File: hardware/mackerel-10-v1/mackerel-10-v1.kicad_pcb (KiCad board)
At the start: 4 copper layers, 150 x 114 mm, 59 parts, among them J1 Conn_02x05_Odd_Even, J10 Conn_01x06, J2 Conn_02x20_Odd_Even, J3 Conn_02x20_Odd_Even, J6 Barrel_Jack_MountingPin, J9 Conn_01x06, SW1 SW_Push, U1 68010D, U3 SST39SF040, U4 AS6C4008-55PCN, U5 SST39SF040, U6 AS6C4008-55PCN, U7 XR68C681, U9 NE555P, X1 50 MHz, X2 3.6864MHz

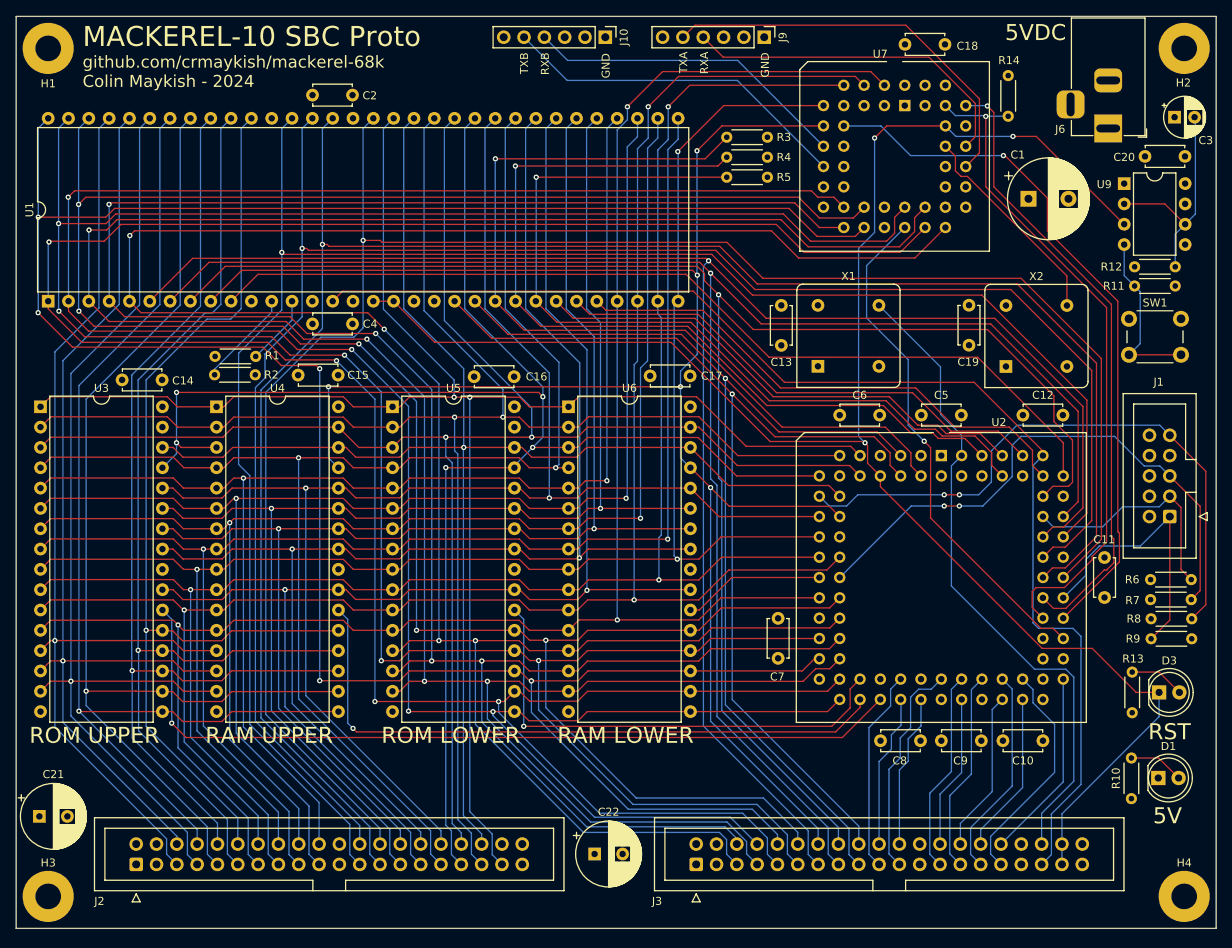
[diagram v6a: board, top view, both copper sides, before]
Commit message: Mack-10 proto routed and passing DRC
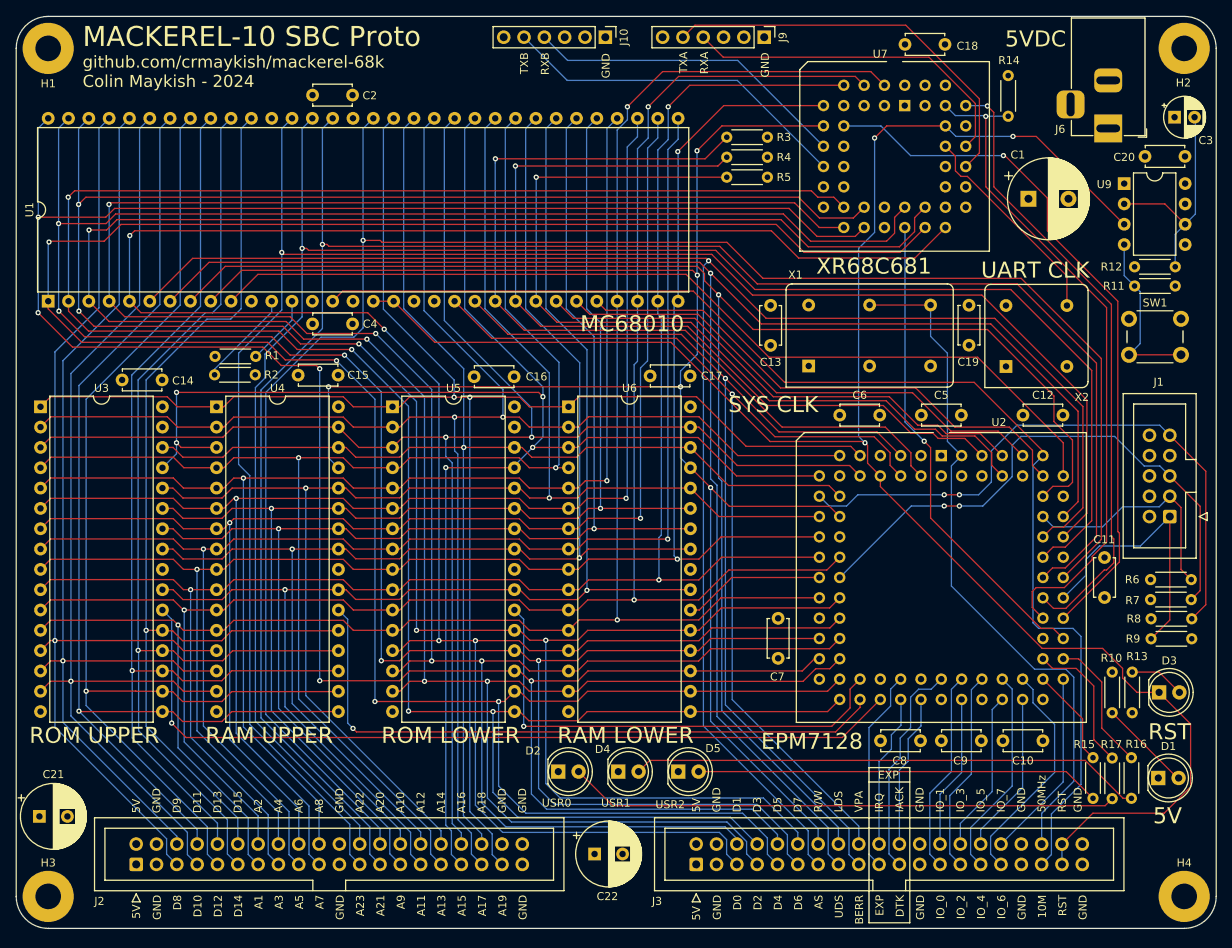
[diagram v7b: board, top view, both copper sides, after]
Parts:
- added D2: LED, LED_THT:LED_D5.0mm, F.Cu at (87.8, 114.4)
- added D4: LED, LED_THT:LED_D5.0mm, F.Cu at (95.3, 114.4)
- added D5: LED, LED_THT:LED_D5.0mm, F.Cu at (102.8, 114.4)
- added R15: R, Resistor_THT:R_Axial_DIN0204_L3.6mm_D1.6mm_P5.08mm_Horizontal, F.Cu at (154.6, 112.7)
- added R16: R, Resistor_THT:R_Axial_DIN0204_L3.6mm_D1.6mm_P5.08mm_Horizontal, F.Cu at (159.4, 112.7)
- added R17: R, Resistor_THT:R_Axial_DIN0204_L3.6mm_D1.6mm_P5.08mm_Horizontal, F.Cu at (157.0, 112.7)
- X1: value 50 MHz -> 50MHz; footprint Oscillator:Oscillator_DIP-8 -> Oscillator:Oscillator_DIP-14
- moved R10 16.0 mm to (157.0, 102.0), turned to -90 degrees
- moved C13 1.34 mm to (114.3, 56.1)
- moved X1 1.16 mm to (119.1, 63.7)
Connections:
- J2 pad 38: unconnected-(J2-Pin_38-Pad38) -> GND
- U2 pad 55: unconnected-(U2-IO-Pad55) -> Net-(R15-Pad1)
- U2 pad 56: unconnected-(U2-IO-Pad56) -> Net-(R16-Pad1)
- U2 pad 57: unconnected-(U2-IO-Pad57) -> Net-(R17-Pad1)
- U7 pad 3: unconnected-(U7-IP3-Pad3) -> GND
- U7 pad 40: unconnected-(U7-IP2-Pad40) -> GND
- U7 pad 42: unconnected-(U7-IP5-Pad42) -> GND
- U7 pad 43: unconnected-(U7-IP4-Pad43) -> GND
- U7 pad 5: unconnected-(U7-IP1-Pad5) -> GND
- U7 pad 8: unconnected-(U7-IP0-Pad8) -> GND
- X1 pad 8: +5V -> CLK_SRC
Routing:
- net USR2: track 0.00 -> 68.8 mm
- net USR1: track 0.00 -> 64.1 mm
- net USR0: track 0.00 -> 50.7 mm
- net Net-(R17-Pad1): track 0.00 -> 17.7 mm
- net Net-(R16-Pad1): track 0.00 -> 17.0 mm
- net Net-(R15-Pad1): track 0.00 -> 12.4 mm
- net /RESET: track 223.3 -> 232.5 mm
- net D5: track 314.4 -> 320.3 mm
- net D0: track 298.5 -> 304.5 mm
- net D1: track 289.0 -> 294.9 mm
- net D2: track 306.4 -> 312.2 mm
- net D6: track 318.2 -> 324.0 mm
- net D3: track 293.6 -> 299.2 mm
- net D7: track 303.8 -> 309.3 mm
- net D4: track 310.4 -> 315.8 mm
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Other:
- outline, holes or cut-outs redrawn
- board text added: "10M"
- board text added: "50MHz"
- board text added: "A1"
- board text added: "A10"
- board text added: "A11"
- board text added: "A12"
- board text added: "A13"
- board text added: "A14"
- board text added: "A15"
- board text added: "A16"
- board text added: "A17"
- board text added: "A18"
- board text added: "A19"
- board text added: "A2"
- board text added: "A20"
- board text added: "A21"
- board text added: "A22"
- board text added: "A23"
- board text added: "A3"
- board text added: "A4"
- board text added: "A5"
- board text added: "A6"
- board text added: "A7"
- board text added: "A8"
- board text added: "A9"
- board text added: "AS"
- board text added: "BERR"
- board text added: "D0"
- board text added: "D1"
- board text added: "D10"
- board text added: "D11"
- board text added: "D12"
- board text added: "D13"
- board text added: "D14"
- board text added: "D15"
- board text added: "D2"
- board text added: "D3"
- board text added: "D4"
- board text added: "D5"
- board text added: "D6"
- board text added: "D7"
- board text added: "D8"
- board text added: "D9"
- board text added: "DTK"
- board text added: "EPM7128"
- board text added: "EXP"
- board text added: "IACK"
- board text added: "IO_0"
- board text added: "IO_1"
- board text added: "IO_2"
- board text added: "IO_3"
- board text added: "IO_4"
- board text added: "IO_5"
- board text added: "IO_6"
- board text added: "IO_7"
- board text added: "IRQ"
- board text added: "LDS"
- board text added: "MC68010"
- board text added: "R/W"
- board text added: "SYS CLK"
- board text added: "UART CLK"
- board text added: "UDS"
- board text added: "USR0"
- board text added: "USR1"
- board text added: "USR2"
- board text added: "VPA"
- board text added: "XR68C681"

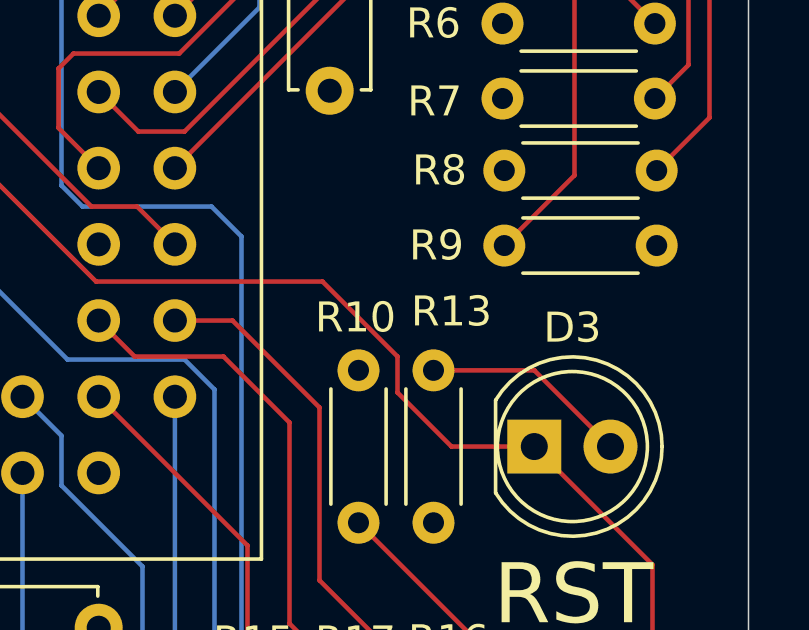
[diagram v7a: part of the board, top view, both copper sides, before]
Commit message: Mackerel-10 proto board ready for manufacturing
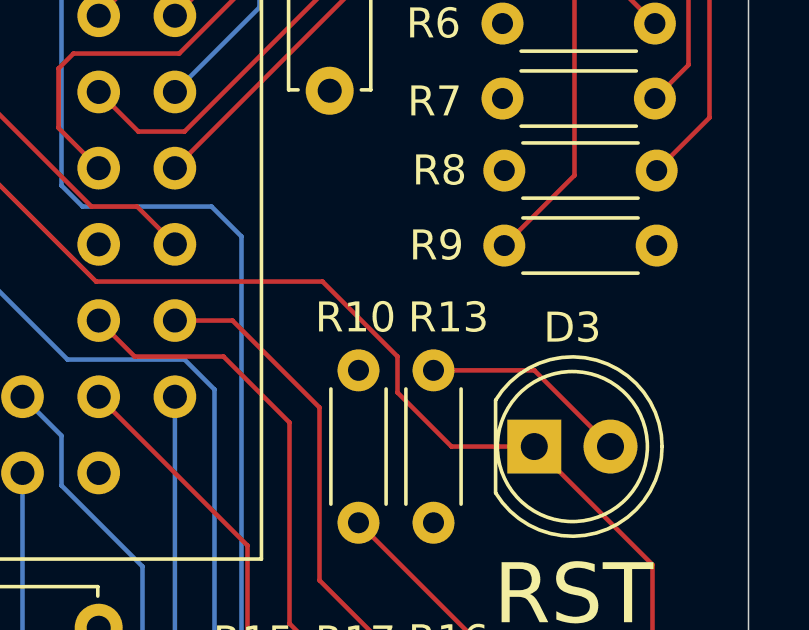
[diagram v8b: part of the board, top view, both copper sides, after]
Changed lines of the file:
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@@
 	)
 	(paper "USLetter")
+	(title_block
+		(title "Mackerel-10 SBC Proto")
+		(date "2024-08-22")
+		(rev "0.1")
+		(company "Colin Maykish")
+	)
 	(layers
 		(0 "F.Cu" signal)
@@
 			(plot_on_all_layers_selection 0x0000000_00000000)
 			(disableapertmacros no)
-			(usegerberextensions no)
+			(usegerberextensions yes)
 			(usegerberattributes yes)
 			(usegerberadvancedattributes yes)
@@
 			(plotinvisibletext no)
 			(sketchpadsonfab no)
-			(subtractmaskfromsilk no)
+			(subtractmaskfromsilk yes)
 			(outputformat 1)
 			(mirror no)
-			(drillshape 1)
+			(drillshape 0)
 			(scaleselection 1)
-			(outputdirectory "")
+			(outputdirectory "/home/colin/Desktop/mack-10-proto/")
 		)
 	)
@@
 		(tags "Resistor Axial_DIN0204 series Axial Horizontal pin pitch 5.08mm 0.167W length 3.6mm diameter 1.6mm")
 		(property "Reference" "R13"
-			(at 7.04 0.6 180)
+			(at 6.84 0.5 180)
 			(layer "F.SilkS")
 			(effects
@@
 		(tags "Resistor Axial_DIN0204 series Axial Horizontal pin pitch 5.08mm 0.167W length 3.6mm diameter 1.6mm")
 		(property "Reference" "R10"
-			(at -1.76 0.1 360)
+			(at -1.76 0.1 0)
 			(layer "F.SilkS")
 			(effects
